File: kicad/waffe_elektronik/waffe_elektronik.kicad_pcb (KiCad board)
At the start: 4 copper layers, 54 x 46 mm, 65 parts, among them J1 WS2812 HP-Streifen, J2 GX16 7-polig, J3 USB-C (Flashen + Laden), M1 Vibromotor Rückstoss, M2 Vibromotor Treffer, Q1 AO3400A, Q2 AO3400A, Q3 AO3400A, SW1 Taster, SW2 Taster, SW3 RESET, SW4 BOOT, U1 MT3608, U12 USBLC6-2SC6, U2 AMS1117-3.3, U3 MCP73831, U4 ESP32-S3-WROOM-1-N16R8, U5 74AHCT125, U6 MAX98357A

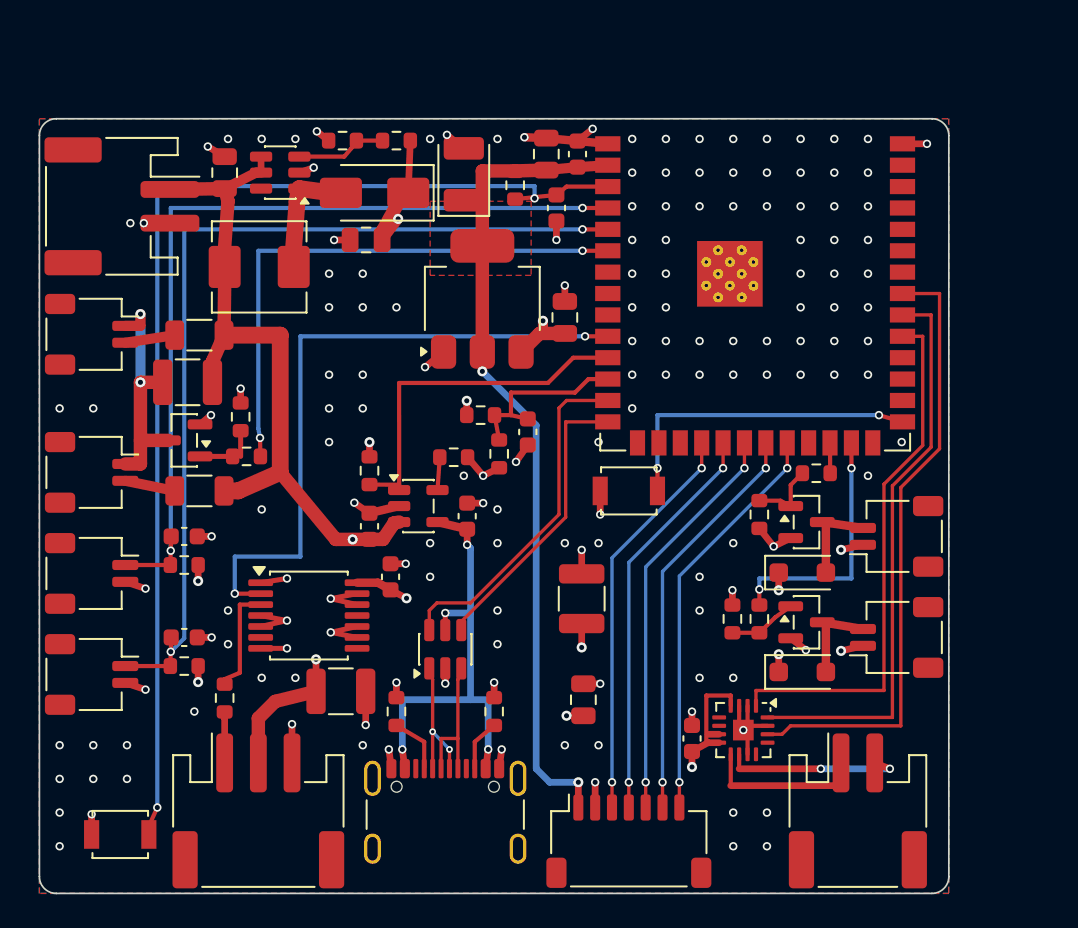
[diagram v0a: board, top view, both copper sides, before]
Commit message: Platine: Leiterbahnen nur 0/45/90 Grad, Knicke max. 45 Grad, Teardrops an Pads und Vias
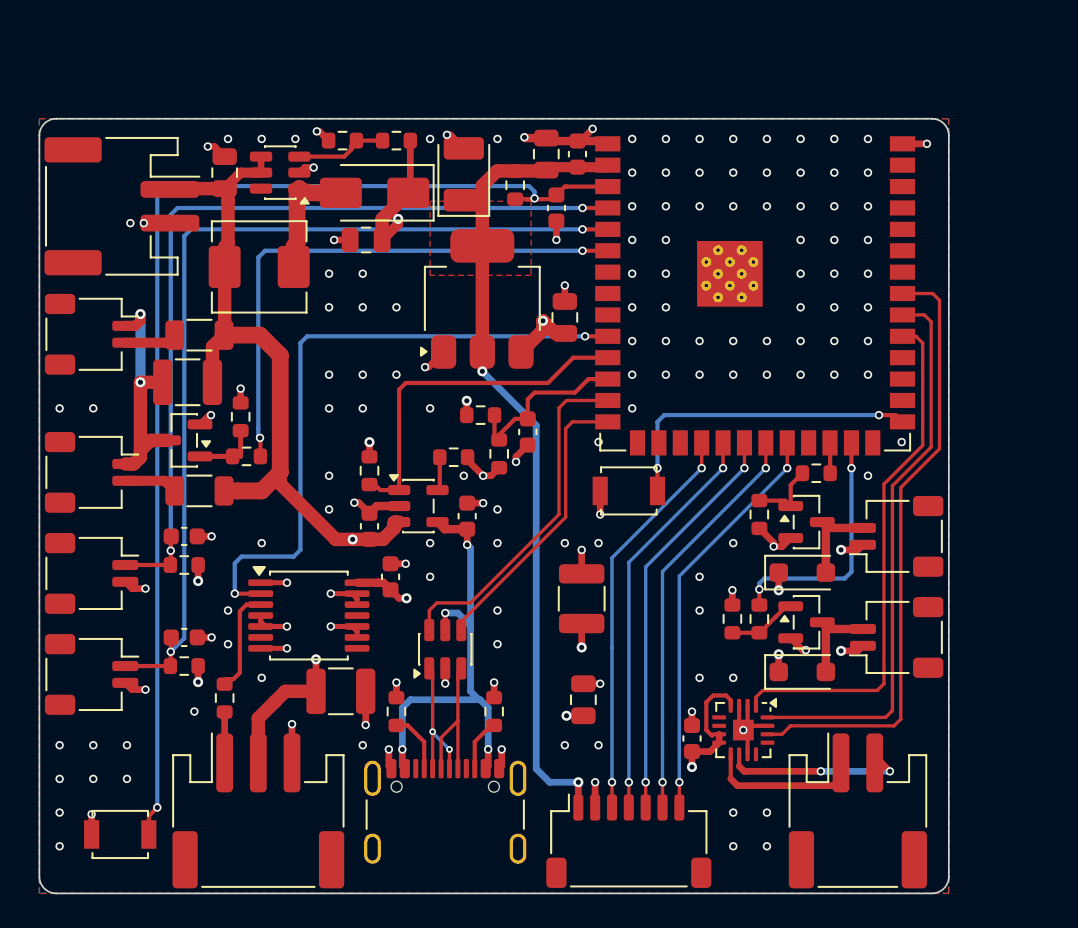
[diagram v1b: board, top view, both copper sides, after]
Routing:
- net GND: track 69.4 -> 67.4 mm, vias 157 -> 159
- net /WS2812_DIN_3V3: track 39.0 -> 38.3 mm
- net /I2S_DOUT: track 31.7 -> 31.0 mm
- net 3V3_MCU: track 77.5 -> 78.2 mm
- net BAT_P: track 52.1 -> 52.7 mm
- net /ADC_BATT: track 10.9 -> 10.4 mm
- net Net-(J3-D+-PadA6): track 8.77 -> 9.29 mm
- net Net-(U6-OUTP): track 9.76 -> 9.25 mm

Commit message: JLCPCB-Bestellpaket: LCSC-Teile im Schaltplan, Gerber/BOM/CPL, Skill jlcpcb-order
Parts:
- L1: value 22u -> 10u
- U5: value 74AHCT125 -> 74HCT125

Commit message: Platine: kürzere Leiterbahnen, Beschriftung auf der Vorderseite
- B.Cu: L-förmige Bahnen durch 45°-Abschnitte ersetzt (EN/Abzug/Nachladen/IR/WS2812
  als paralleles Bündel, BOOT, Rückstoß, 3V3-Sensor), VBUS-Ring mit 45°-Ecken
- Steckerbeschriftung auf F.SilkS neben dem jeweiligen Stecker, frei von Pads
  und Bauteilkörpern; Pin 1 von J2 markiert; Projekt-URL auf B.SilkS
- Skill kicad-pcb: Regeln "so kurz wie möglich" und "Beschriftung vorne",
  Prüfwerkzeuge tools/detour.py und tools/silk.py
- Fertigungsdaten JLCPCB neu erzeugt, BOM-Kommentare stabil sortiert
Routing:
- net Net-(U4-EN): track 67.2 -> 56.7 mm
- net /TRIGGER: track 50.5 -> 40.6 mm
- net /RELOAD: track 54.7 -> 45.6 mm
- net /WS2812_DIN_3V3: track 38.3 -> 30.0 mm
- net /IR_GATE: track 32.8 -> 26.4 mm
- net /RECOIL_VIB: track 14.7 -> 11.9 mm
- net Net-(U4-IO0): track 19.0 -> 17.4 mm
- net 3V3_MCU: track 78.2 -> 77.2 mm
- net GND: vias 159 -> 163
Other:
- board text added: "1"
- board text removed: "1 3V3 2 GND 3-7 TSOP1-5"

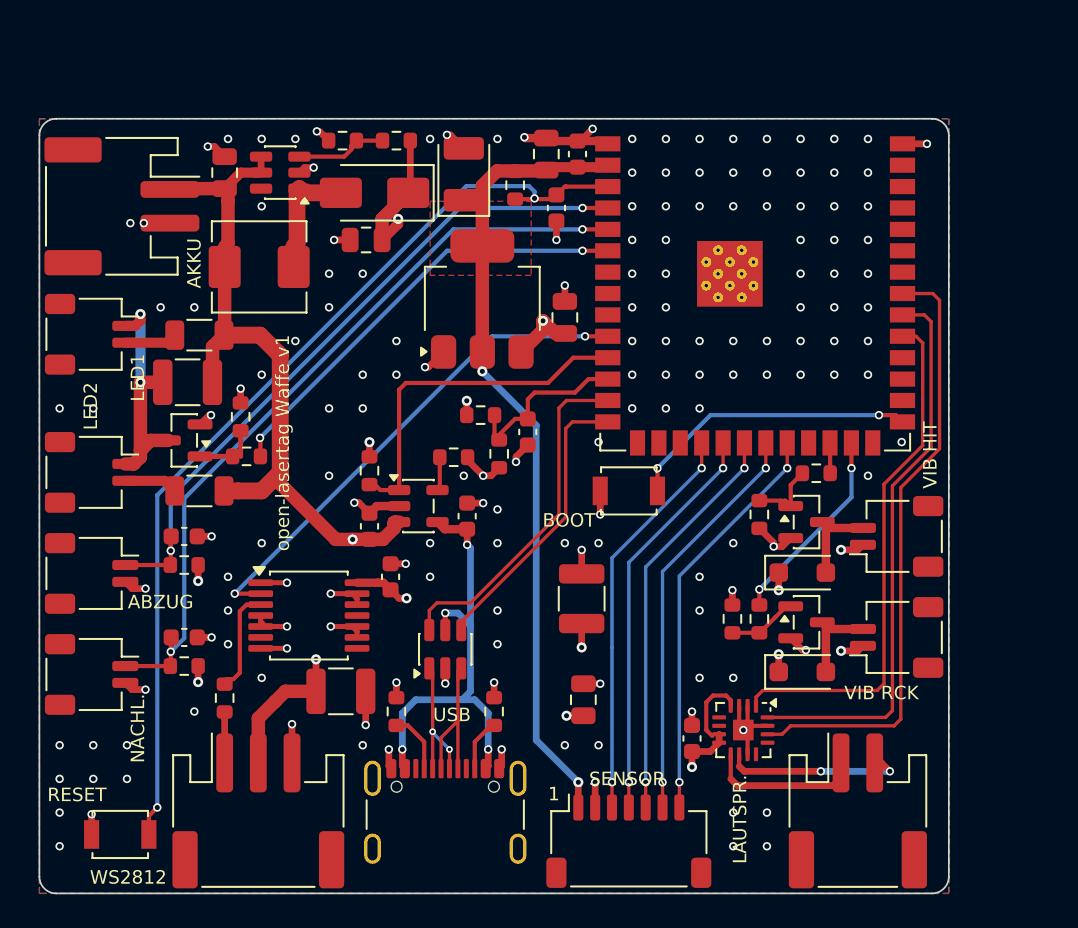
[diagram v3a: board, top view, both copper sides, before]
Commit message: Platine: kürzeste Leiterbahnen, USB-Paar längenangepasst, Labels ausgerichtet, 3D-Modelle
- Leiterbahnen auf F.Cu und In2 verkürzt (CHRG_STAT, ADC_BATT, BAT_P, 3V3, 5V-Äste u. a.)
- USB D+ mit Mäander, D+/D- je Abschnitt gleich lang
- Labels waagerecht, Steckerspalten auf gemeinsamer Mittelachse, untere Stecker mittig;
  keine Vias unter Labels, Stitching hält Textflächen frei
- Eigene 3D-Modelle für JST-PH-SM4 (BT1, SP1, J1), erzeugt mit FreeCAD
- Skill kicad-pcb: Regeln und Werkzeuge pairlen.py, silk.py --column/--row, detour.py
- Renders und JLCPCB-Fertigungsdaten neu erzeugt
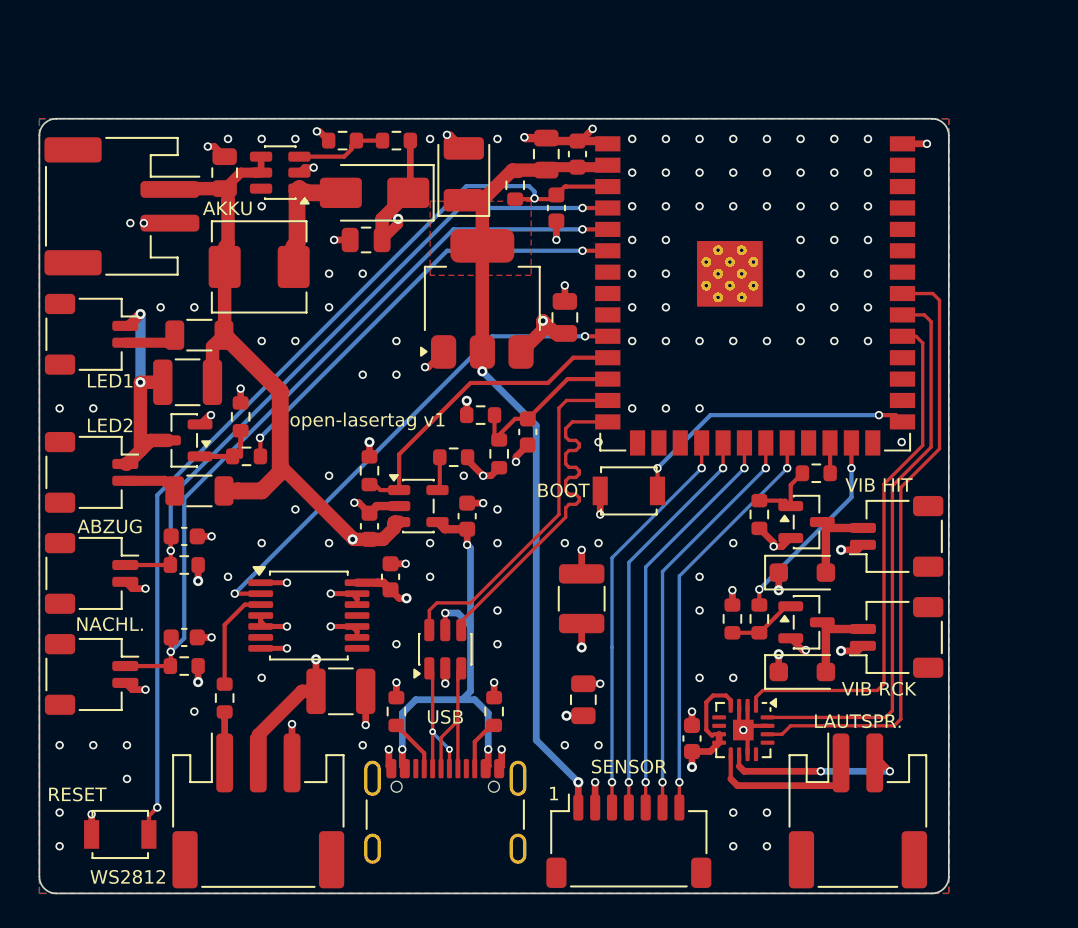
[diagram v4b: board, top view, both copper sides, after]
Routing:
- net 5V_PERIPH: track 128.9 -> 124.3 mm
- net /USB_D+: track 17.2 -> 20.6 mm
- net /CHRG_STAT: track 21.0 -> 18.8 mm
- net BAT_P: track 52.7 -> 51.2 mm
- net Net-(U6-OUTP): track 9.25 -> 7.93 mm
- net /ADC_BATT: track 10.4 -> 9.72 mm
- net 3V3_MCU: track 77.2 -> 76.7 mm
- net GND: vias 163 -> 151
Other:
- board text added: "open-lasertag v1"
- board text removed: "open-lasertag Waffe v1"

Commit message: Platine: Befestigung, OLED/Drehgeber, TSOP 6 an der Waffe, ein Vibrationsmotor
- 2 x M2-Befestigungslöcher (ISO 7380), kupferfrei auf allen Lagen
- OLED (I2C, Qwiic, J4) und Drehdrück-Geber (J5) an JST-SH 4 im neuen Streifen
  oben rechts, Platine L-förmig 59,6 x 46 mm
- Zweite TSAL6100 entfällt, an ihrem Platz J6 (JST-SH 3) für TSOP 6 an der Waffe (GPIO16),
  Filter am Sensor
- Nur noch ein Vibrationsmotor (GPIO47), GPIO48 frei; I2S-Leitungen kürzer
- Firmware: Pins für OLED/Geber, TSOP 6 auf GPIO16, ein Motor mit Prioritäten
- Schaltplan, Fertigungsdaten, Renders, Doku und Skills aktualisiert
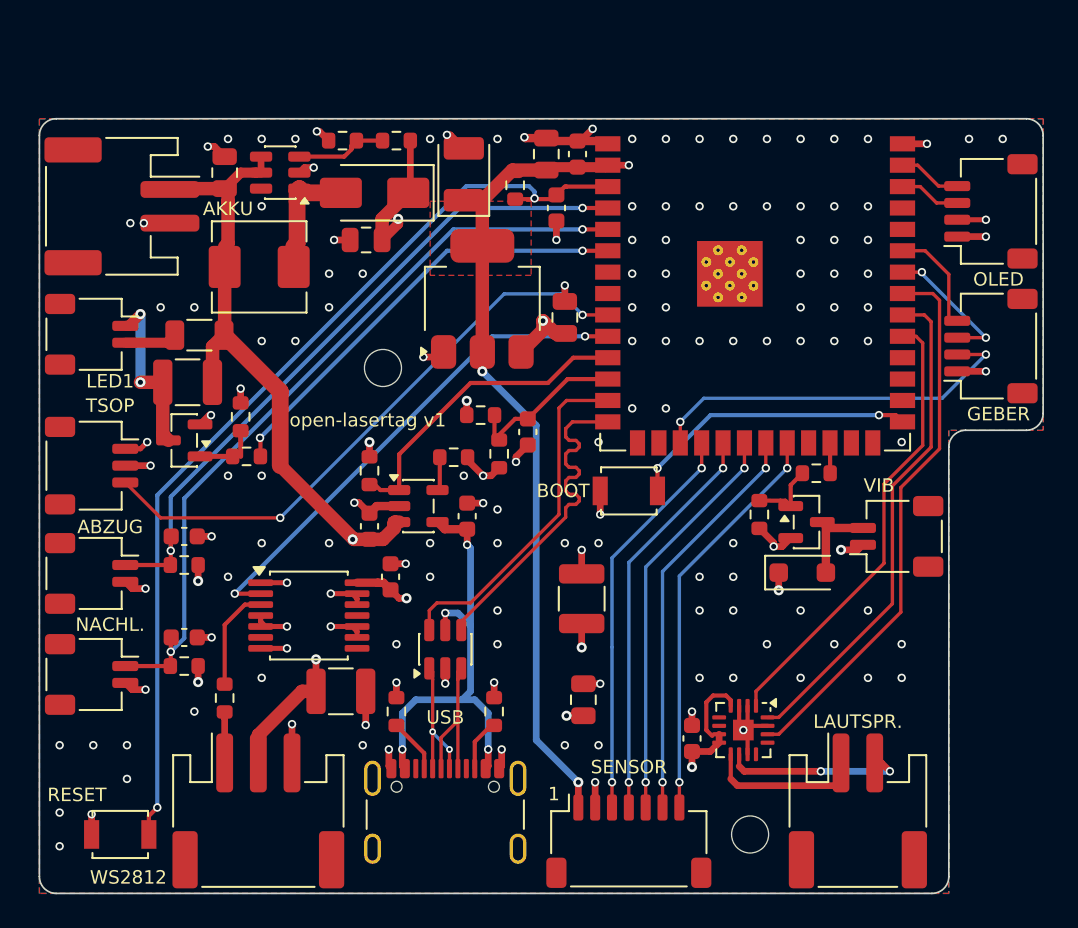
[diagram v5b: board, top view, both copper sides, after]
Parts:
- removed D2: SS14, Diode_SMD:D_SOD-123F
- removed LED2: TSAL6100, Connector_JST:JST_SH_SM02B-SRSS-TB_1x02-1MP_P1.00mm_Horizontal
- removed M2: Vibromotor Treffer, Connector_JST:JST_SH_SM02B-SRSS-TB_1x02-1MP_P1.00mm_Horizontal
- removed Q3: AO3400A, Package_TO_SOT_SMD:SOT-23
- removed R13: 100, Resistor_SMD:R_0603_1608Metric
- removed R14: 100k, Resistor_SMD:R_0603_1608Metric
- removed R8: 10, Resistor_SMD:R_1206_3216Metric
- added H1: M2, MountingHole:MountingHole_2.2mm_M2_ISO7380, F.Cu at (20.4, 14.8)
- added H2: M2, MountingHole:MountingHole_2.2mm_M2_ISO7380, F.Cu at (42.2, 42.5)
- added J4: OLED I²C (Qwiic), Connector_JST:JST_SH_SM04B-SRSS-TB_1x04-1MP_P1.00mm_Horizontal, F.Cu at (56.5, 5.50)
- added J5: Drehgeber, Connector_JST:JST_SH_SM04B-SRSS-TB_1x04-1MP_P1.00mm_Horizontal, F.Cu at (56.5, 13.5)
- added J6: TSOP 6 (Waffe), Connector_JST:JST_SH_SM03B-SRSS-TB_1x03-1MP_P1.00mm_Horizontal, F.Cu at (3.10, 20.6)
- M1: value Vibromotor Rückstoss -> Vibromotor
- moved R11 9.29 mm to (46.1, 21.1), turned to 180 degrees
- moved R12 6.40 mm to (42.8, 23.5), turned to -90 degrees
- moved M1 6.00 mm to (50.9, 24.8)
- moved Q2 5.95 mm to (45.5, 23.9)
- moved D1 5.90 mm to (45.3, 26.9)
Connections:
- R11 pad 1: /RECOIL_VIB -> /VIB
- U4 pad 17: unconnected-(U4-IO9-Pad17) -> /ENC_SW
- U4 pad 24: /HIT_VIB -> /VIB
- U4 pad 25: /RECOIL_VIB -> unconnected-(U4-IO48-Pad25)
- U4 pad 34: unconnected-(U4-IO41-Pad34) -> /ENC_B
- U4 pad 35: unconnected-(U4-IO42-Pad35) -> /ENC_A
- U4 pad 38: unconnected-(U4-IO2-Pad38) -> /I2C_SDA
- U4 pad 39: unconnected-(U4-IO1-Pad39) -> /I2C_SCL
- U4 pad 9: unconnected-(U4-IO16-Pad9) -> /TSOP6_OUT
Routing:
- net 3V3_MCU: track 76.7 -> 114.6 mm, vias 5 -> 8
- net /TSOP6_OUT: track 0.00 -> 35.5 mm, vias 0 -> 2
- net /ENC_SW: track 0.00 -> 22.8 mm, vias 0 -> 2
- net /RECOIL_VIB: track 11.9 -> 0.00 mm, vias 2 -> 0
- net 5V_PERIPH: track 124.3 -> 113.3 mm, vias 11 -> 9
- net /ENC_B: track 0.00 -> 8.31 mm, vias 0 -> 2
- net /ENC_A: track 0.00 -> 6.09 mm
- net Net-(D2-A): track 5.26 -> 0.00 mm
- net Net-(Q3-G): track 4.23 -> 0.00 mm
- net BAT_P: track 51.2 -> 47.1 mm
- net /I2S_DOUT: track 31.0 -> 27.0 mm
- net /I2C_SCL: track 0.00 -> 3.76 mm
- net /I2S_LRCLK: track 36.5 -> 32.8 mm
- net /I2S_BCLK: track 33.5 -> 29.8 mm
- net /I2C_SDA: track 0.00 -> 3.65 mm
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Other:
- board size 54 x 46 mm -> 59.6 x 46 mm
- board text added: "GEBER"
- board text added: "OLED"
- board text added: "TSOP"
- board text added: "VIB"
- board text removed: "LED2"
- board text removed: "VIB HIT"
- board text removed: "VIB RCK"

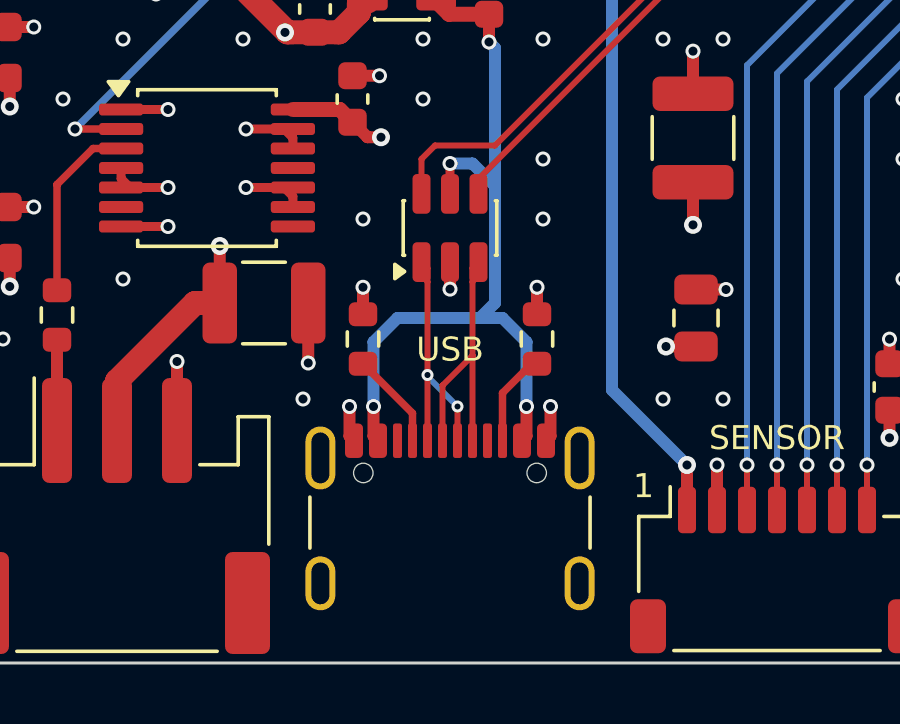
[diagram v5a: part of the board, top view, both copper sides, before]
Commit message: Platine: USB-C senkrecht (HRO TYPE-C-31-E-17), Stecker durch die Seitenwand
- J3 jetzt senkrechte, wasserdichte USB-C-Buchse (LCSC C7424785), eigener Footprint in
  footprints/lasertag.pretty (fp-lib-table), 3D-Modell per gen_3d_usb_c_vertical.py
- USB-Paar neu geroutet: D+ über Via in der Buchsenmitte, D- über B.Cu-Brücke mit Abgriff
  in der Mitte; beide Steckrichtungen gleich lang (<= 0,007 mm), je 2 Vias
- CC2-Widerstand R22 unter der Buchse, R23 daneben; VBUS-Ring auf B.Cu
- Schaltplan, Fertigungsdaten, Renders, Doku und Skill aktualisiert
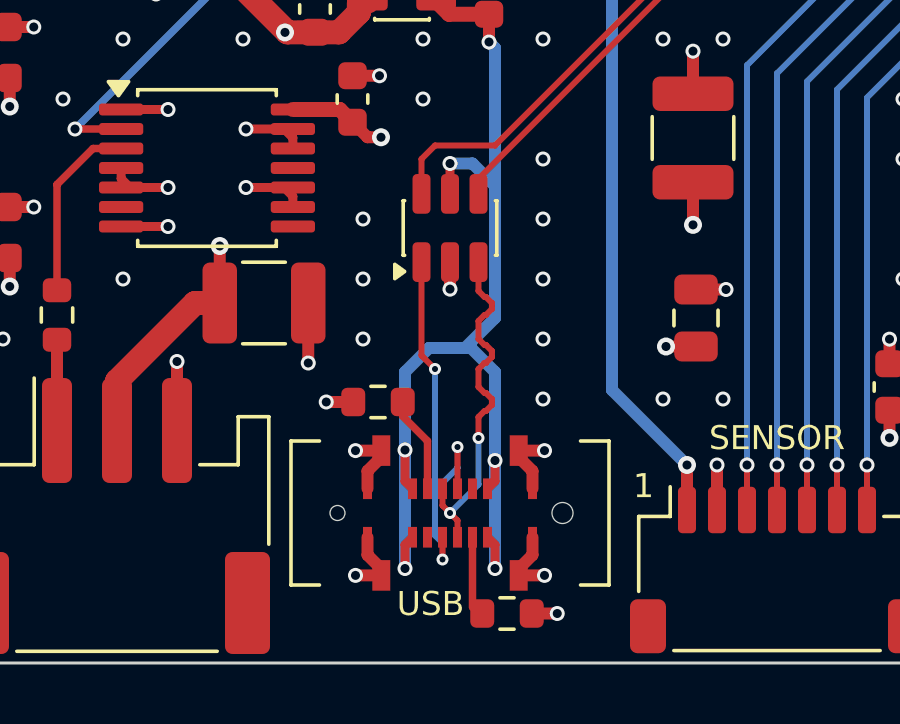
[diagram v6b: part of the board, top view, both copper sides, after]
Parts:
- J3: footprint Connector_USB:USB_C_Receptacle_GCT_USB4105-xx-A_16P_TopMnt_Horizontal -> lasertag:USB_C_Receptacle_HRO_TYPE-C-31-E-17_Vertical
- moved R22 9.20 mm to (26.0, 44.4), turned to 0 degrees
- moved R23 2.16 mm to (21.7, 37.3), turned to 180 degrees
- moved J3 1.27 mm to (24.1, 41.0)
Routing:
- net VBUS_NATIVE: track 27.6 -> 37.9 mm, vias 4 -> 6
- net GND: track 70.1 -> 76.0 mm, vias 146 -> 152
- net Net-(J3-D--PadA7): track 8.64 -> 14.1 mm, vias 2 -> 3
- net Net-(J3-D+-PadA6): track 9.29 -> 11.9 mm, vias 0 -> 2
- net Net-(J3-CC2): track 3.14 -> 2.34 mm
